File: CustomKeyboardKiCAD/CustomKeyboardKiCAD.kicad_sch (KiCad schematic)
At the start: 60 parts, among them J1 USB_C_Receptacle_USB2.0_16P, J2 Display Connector, J3 S2B-PH-K-SLFSN, J4 Conn_01x12, J5 Conn_01x12, J6 USB_C_Receptacle, SW91 RotaryEncoder_Switch, U1 nRF52840, U2 XC6220B331MR, U3 74HC595, U4 BQ24075RGTR, U5 74HC595, U6 74HC595, U7 nice_nano, Y1 32.768kHz FC-12M, Y2 32MHz XRCGB32MOODF1H5ORO

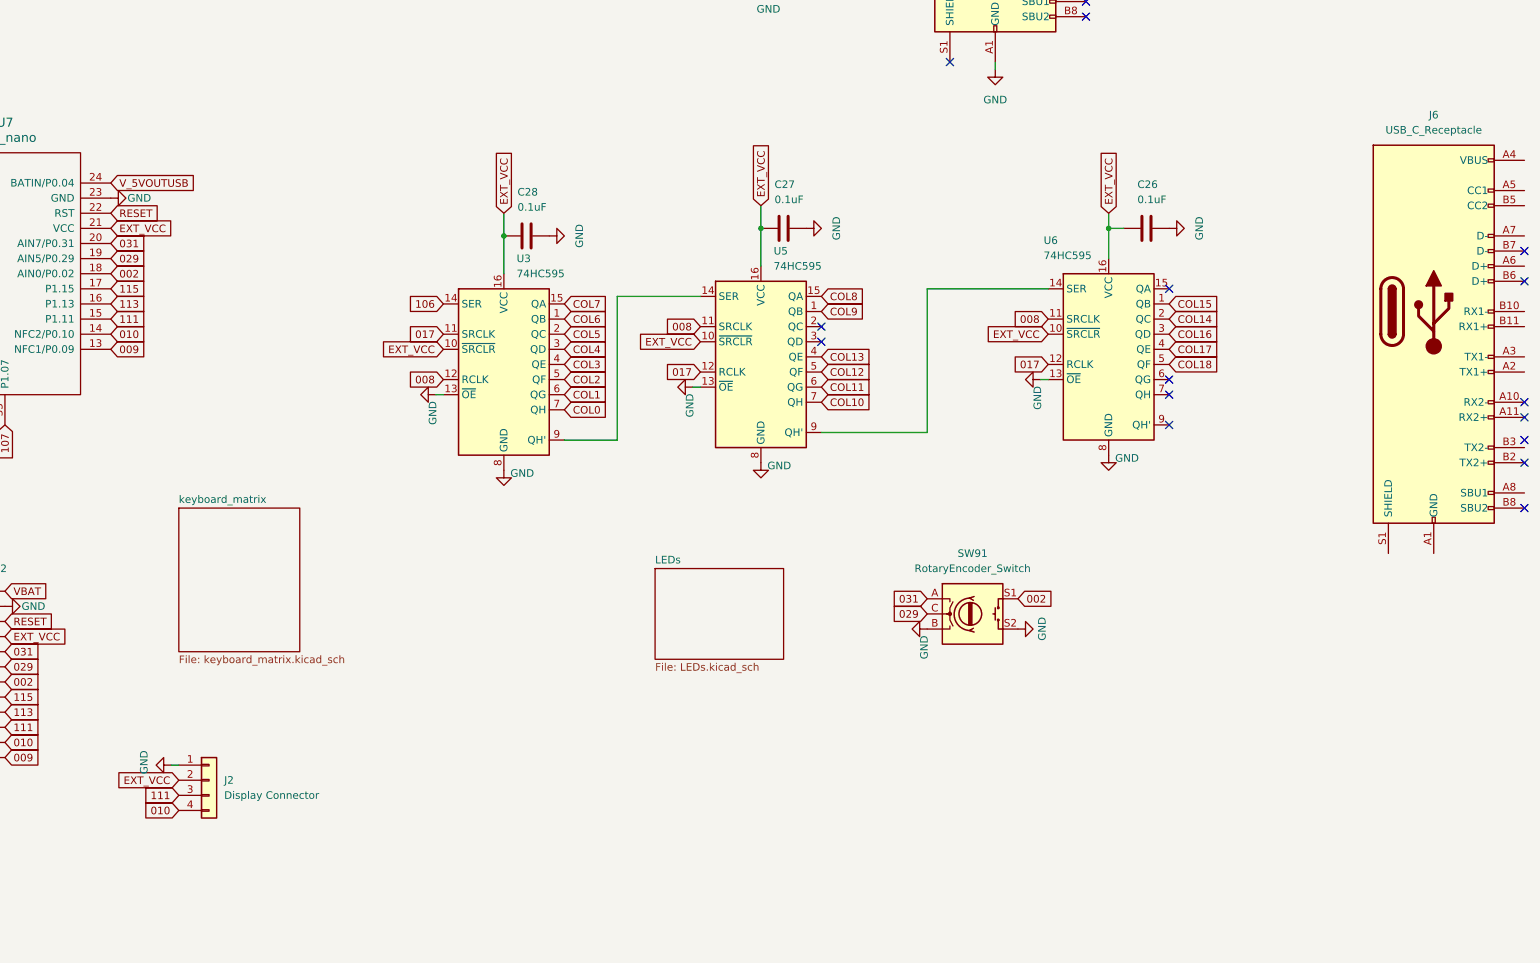
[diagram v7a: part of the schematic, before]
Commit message: added usb hub and 3d models
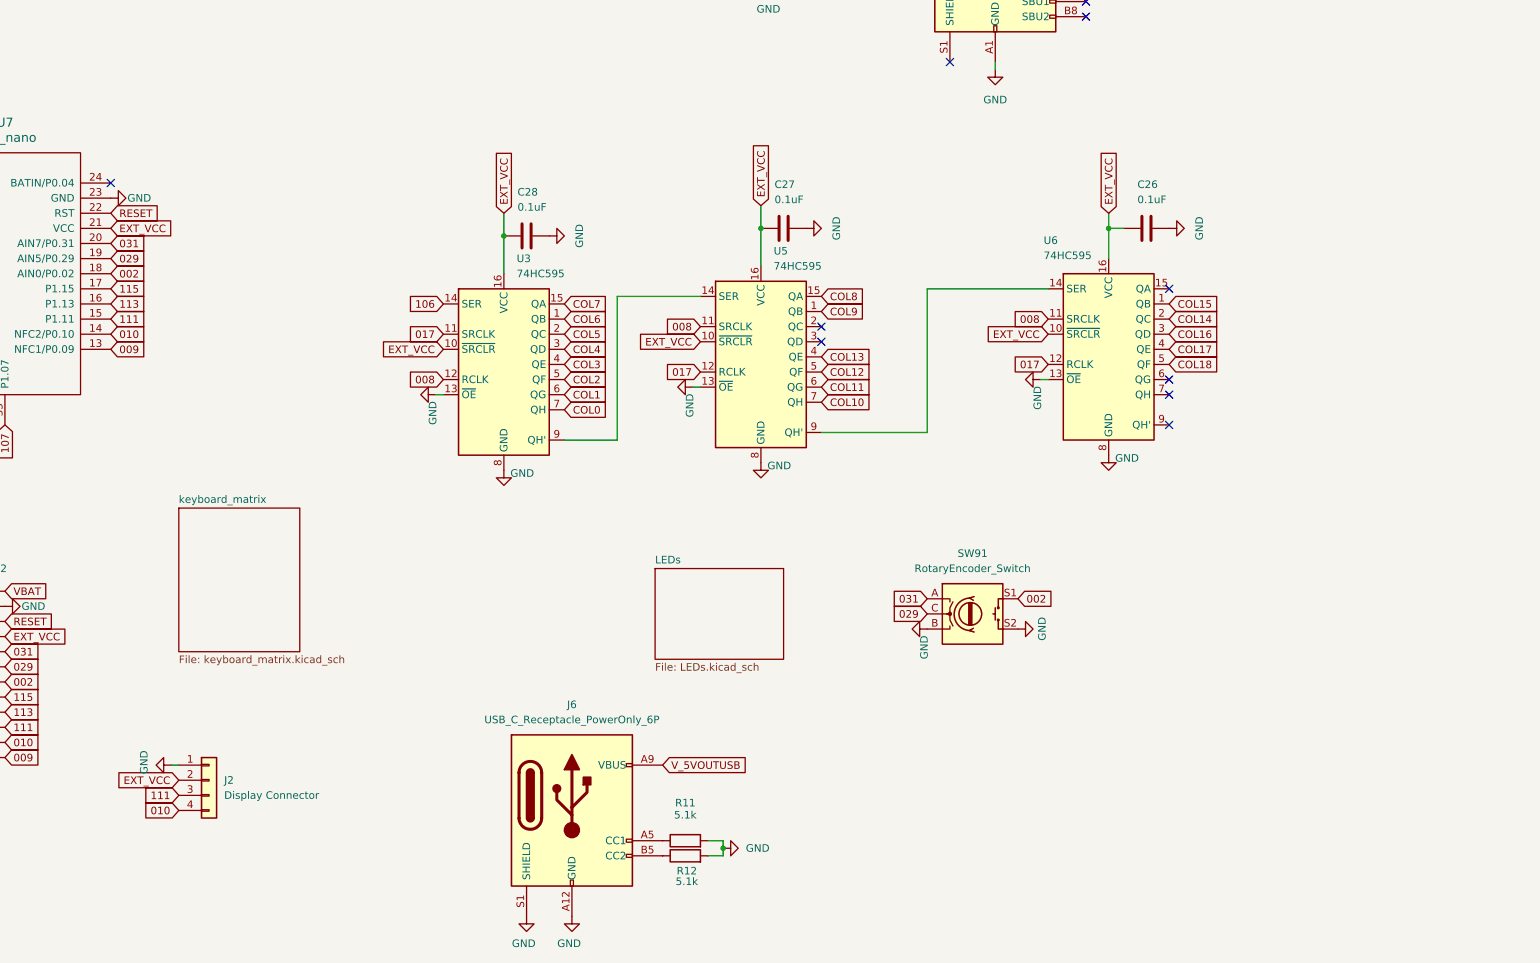
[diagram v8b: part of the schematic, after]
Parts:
- removed J6: USB_C_Receptacle, symbol Connector:USB_C_Receptacle
- added J6: USB_C_Receptacle_PowerOnly_6P, usbrecept:2171750001_MOL, symbol Connector:USB_C_Receptacle_PowerOnly_6P
- added R11, R12: 5.1k, usbresistor:RC0402N_YAG-L, symbol Device:R
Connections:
- net GND: now also J6.A12 (GND), J6.B12 (GND), J6.S1 (SHIELD), R11.2, R12.2
- net V_5VOUTUSB: now also J6.A9 (VBUS), J6.B9 (VBUS); no longer U7.24 (BATIN/P0.04)
- new net: J6.A5 (CC1), R11.1
- new net: J6.B5 (CC2), R12.1
- no-connect marks 38 -> 32
